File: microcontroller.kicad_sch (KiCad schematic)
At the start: 22 parts, among them J1 TC2030-IDC, U1 ESP32-WROVER

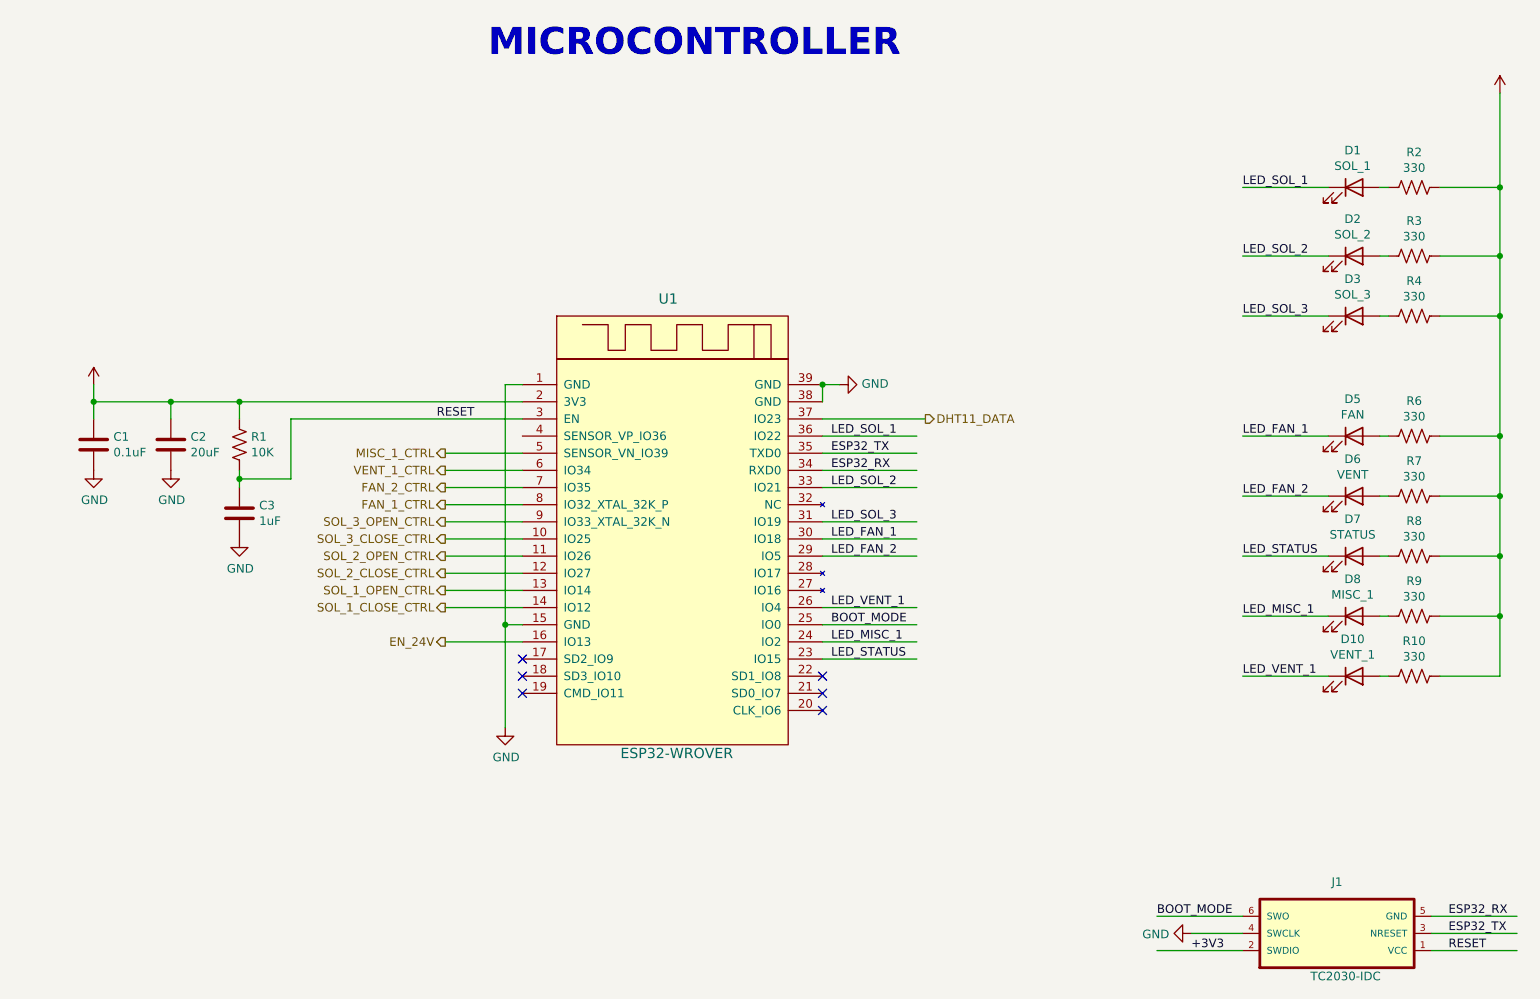
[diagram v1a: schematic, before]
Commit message: Added clamping diode for 24V net.
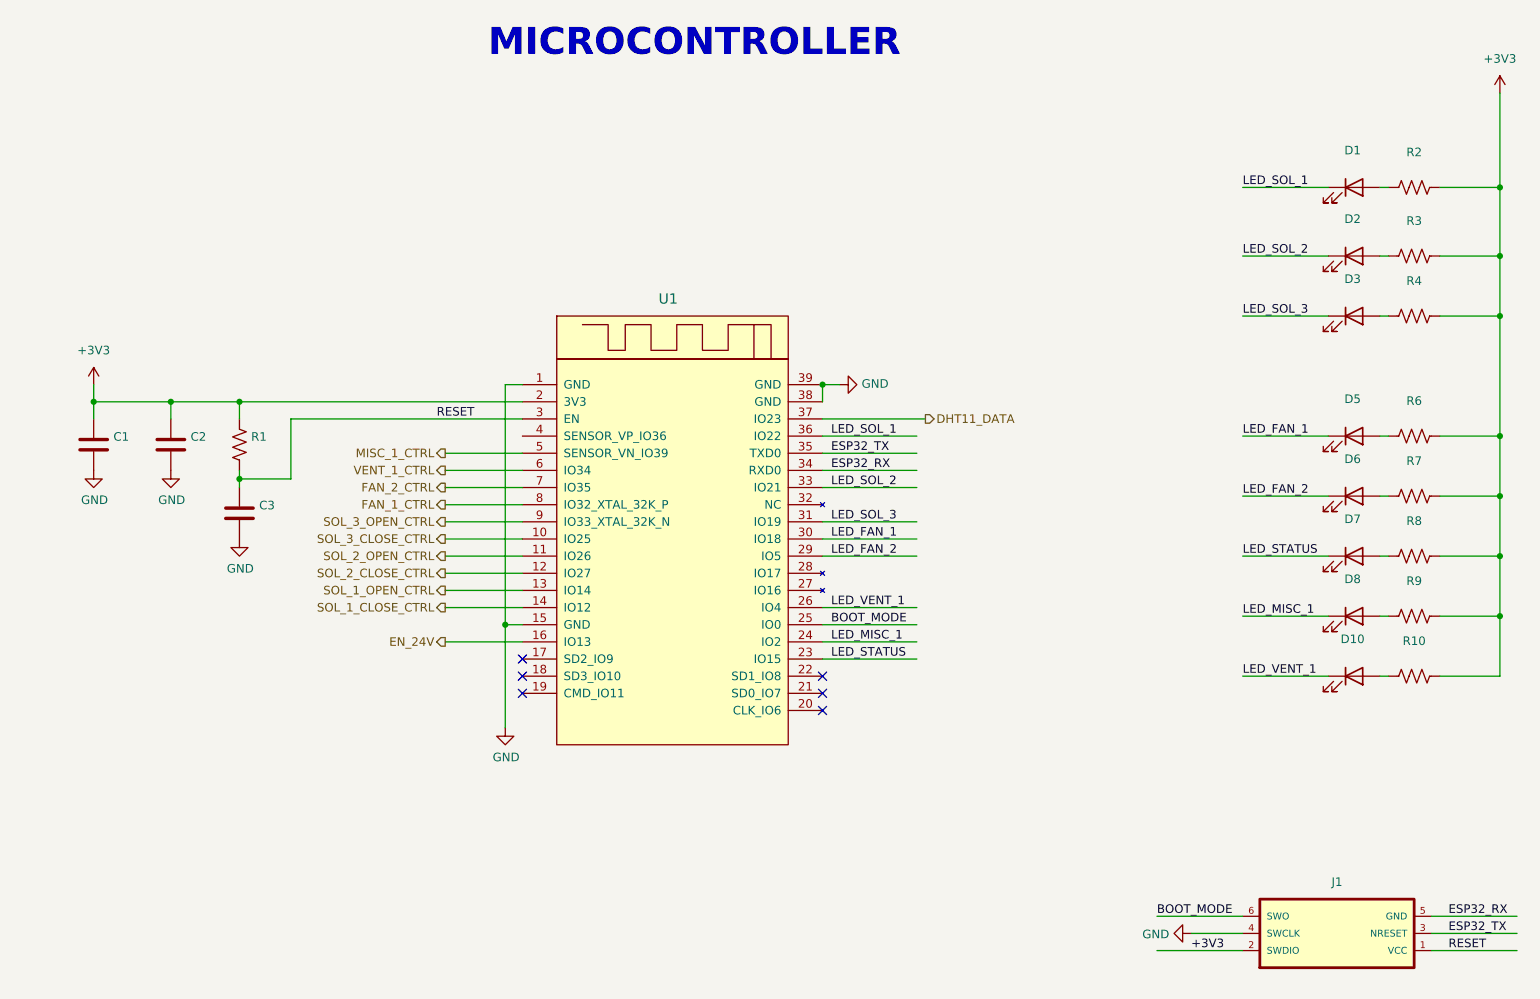
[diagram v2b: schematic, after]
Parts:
- C1: value 0.1uF -> (none); footprint Capacitor_SMD:C_0805_2012Metric -> (none)
- C2: value 20uF -> (none); footprint Capacitor_SMD:C_0805_2012Metric -> (none)
- C3: value 1uF -> (none); footprint Capacitor_SMD:C_0805_2012Metric -> (none)
- D1: value SOL_1 -> (none); footprint LED_SMD:LED_0805_2012Metric -> (none)
- D10: value VENT_1 -> (none); footprint LED_SMD:LED_0805_2012Metric -> (none)
- D2: value SOL_2 -> (none); footprint LED_SMD:LED_0805_2012Metric -> (none)
- D3: value SOL_3 -> (none); footprint LED_SMD:LED_0805_2012Metric -> (none)
- D5: value FAN -> (none); footprint LED_SMD:LED_0805_2012Metric -> (none)
- D6: value VENT -> (none); footprint LED_SMD:LED_0805_2012Metric -> (none)
- D7: value STATUS -> (none); footprint LED_SMD:LED_0805_2012Metric -> (none)
- D8: value MISC_1 -> (none); footprint LED_SMD:LED_0805_2012Metric -> (none)
- J1: value TC2030-IDC -> (none); footprint connector:TC2030-IDC -> (none)
- R1: value 10K -> (none); footprint Resistor_SMD:R_0805_2012Metric -> (none)
- R10, R2, R3, R4, R6, R7, R8, R9: value 330 -> (none); footprint Resistor_SMD:R_0805_2012Metric -> (none)
- U1: value ESP32-WROVER -> (none); footprint esp32-wrover:ESP32-WROVER -> (none)
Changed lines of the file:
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@@
       (effects (font (size 1.524 1.524)))
     )
-    (property "Value" "ESP32-WROVER" (id 1) (at 153.67 128.27 0)
+    (property "Value" "" (id 1) (at 153.67 128.27 0)
       (effects (font (size 1.524 1.524)))
     )
-    (property "Footprint" "esp32-wrover:ESP32-WROVER" (id 2) (at 165.1 100.33 0)
+    (property "Footprint" "" (id 2) (at 165.1 100.33 0)
       (effects (font (size 1.524 1.524)) hide)
     )
@@
       (effects (font (size 1.27 1.27)) (justify left))
     )
-    (property "Value" "20uF" (id 1) (at 81.661 83.693 0)
-      (effects (font (size 1.27 1.27)) (justify left))
-    )
-    (property "Footprint" "Capacitor_SMD:C_0805_2012Metric" (id 2) (at 79.7052 86.36 0)
+    (property "Value" "" (id 1) (at 81.661 83.693 0)
+      (effects (font (size 1.27 1.27)) (justify left))
+    )
+    (property "Footprint" "" (id 2) (at 79.7052 86.36 0)
       (effects (font (size 1.27 1.27)) hide)
     )
@@
       (effects (font (size 1.27 1.27)) (justify left))
     )
-    (property "Value" "0.1uF" (id 1) (at 70.231 83.693 0)
-      (effects (font (size 1.27 1.27)) (justify left))
-    )
-    (property "Footprint" "Capacitor_SMD:C_0805_2012Metric" (id 2) (at 68.2752 86.36 0)
+    (property "Value" "" (id 1) (at 70.231 83.693 0)
+      (effects (font (size 1.27 1.27)) (justify left))
+    )
+    (property "Footprint" "" (id 2) (at 68.2752 86.36 0)
       (effects (font (size 1.27 1.27)) hide)
     )
@@
     (in_bom yes) (on_board yes)
     (property "Reference" "D1" (id 0) (at 253.7714 38.9636 0))
-    (property "Value" "SOL_1" (id 1) (at 253.7714 41.275 0))
-    (property "Footprint" "LED_SMD:LED_0805_2012Metric" (id 2) (at 254 44.45 0)
+    (property "Value" "" (id 1) (at 253.7714 41.275 0))
+    (property "Footprint" "" (id 2) (at 254 44.45 0)
       (effects (font (size 1.27 1.27)) hide)
     )
@@
     (in_bom yes) (on_board yes)
     (property "Reference" "D2" (id 0) (at 253.7714 49.1236 0))
-    (property "Value" "SOL_2" (id 1) (at 253.7714 51.435 0))
-    (property "Footprint" "LED_SMD:LED_0805_2012Metric" (id 2) (at 254 54.61 0)
+    (property "Value" "" (id 1) (at 253.7714 51.435 0))
+    (property "Footprint" "" (id 2) (at 254 54.61 0)
       (effects (font (size 1.27 1.27)) hide)
     )
@@
     (in_bom yes) (on_board yes)
     (property "Reference" "D3" (id 0) (at 253.7714 58.0136 0))
-    (property "Value" "SOL_3" (id 1) (at 253.7714 60.325 0))
-    (property "Footprint" "LED_SMD:LED_0805_2012Metric" (id 2) (at 254 63.5 0)
+    (property "Value" "" (id 1) (at 253.7714 60.325 0))
+    (property "Footprint" "" (id 2) (at 254 63.5 0)
       (effects (font (size 1.27 1.27)) hide)
     )
@@
     (in_bom yes) (on_board yes)
     (property "Reference" "D5" (id 0) (at 253.7714 75.7936 0))
-    (property "Value" "FAN" (id 1) (at 253.7714 78.105 0))
-    (property "Footprint" "LED_SMD:LED_0805_2012Metric" (id 2) (at 254 81.28 0)
+    (property "Value" "" (id 1) (at 253.7714 78.105 0))
+    (property "Footprint" "" (id 2) (at 254 81.28 0)
       (effects (font (size 1.27 1.27)) hide)
     )
@@
     (in_bom yes) (on_board yes)
     (property "Reference" "D6" (id 0) (at 253.7714 84.6836 0))
-    (property "Value" "VENT" (id 1) (at 253.7714 86.995 0))
-    (property "Footprint" "LED_SMD:LED_0805_2012Metric" (id 2) (at 254 90.17 0)
+    (property "Value" "" (id 1) (at 253.7714 86.995 0))
+    (property "Footprint" "" (id 2) (at 254 90.17 0)
       (effects (font (size 1.27 1.27)) hide)
     )
@@
     (in_bom yes) (on_board yes)
     (property "Reference" "D7" (id 0) (at 253.7714 93.5736 0))
-    (property "Value" "STATUS" (id 1) (at 253.7714 95.885 0))
-    (property "Footprint" "LED_SMD:LED_0805_2012Metric" (id 2) (at 254 99.06 0)
+    (property "Value" "" (id 1) (at 253.7714 95.885 0))
+    (property "Footprint" "" (id 2) (at 254 99.06 0)
       (effects (font (size 1.27 1.27)) hide)
     )
@@
       (effects (font (size 1.27 1.27)) (justify left))
     )
-    (property "Value" "1uF" (id 1) (at 91.821 93.853 0)
-      (effects (font (size 1.27 1.27)) (justify left))
-    )
-    (property "Footprint" "Capacitor_SMD:C_0805_2012Metric" (id 2) (at 89.8652 96.52 0)
+    (property "Value" "" (id 1) (at 91.821 93.853 0)
+      (effects (font (size 1.27 1.27)) (justify left))
+    )
+    (property "Footprint" "" (id 2) (at 89.8652 96.52 0)
       (effects (font (size 1.27 1.27)) hide)
     )
@@
       (effects (font (size 1.27 1.27)) (justify left))
     )
-    (property "Value" "10K" (id 1) (at 90.6272 83.693 0)
-      (effects (font (size 1.27 1.27)) (justify left))
-    )
-    (property "Footprint" "Resistor_SMD:R_0805_2012Metric" (id 2) (at 89.916 82.804 90)
+    (property "Value" "" (id 1) (at 90.6272 83.693 0)
+      (effects (font (size 1.27 1.27)) (justify left))
+    )
+    (property "Footprint" "" (id 2) (at 89.916 82.804 90)
       (effects (font (size 1.27 1.27)) hide)
     )
@@
     (in_bom yes) (on_board yes)
     (property "Reference" "R2" (id 0) (at 262.89 39.243 90))
-    (property "Value" "330" (id 1) (at 262.89 41.5544 90))
-    (property "Footprint" "Resistor_SMD:R_0805_2012Metric" (id 2) (at 262.636 45.466 90)
+    (property "Value" "" (id 1) (at 262.89 41.5544 90))
+    (property "Footprint" "" (id 2) (at 262.636 45.466 90)
       (effects (font (size 1.27 1.27)) hide)
     )
@@
     (in_bom yes) (on_board yes)
     (property "Reference" "R6" (id 0) (at 262.89 76.073 90))
-    (property "Value" "330" (id 1) (at 262.89 78.3844 90))
-    (property "Footprint" "Resistor_SMD:R_0805_2012Metric" (id 2) (at 262.636 82.296 90)
+    (property "Value" "" (id 1) (at 262.89 78.3844 90))
+    (property "Footprint" "" (id 2) (at 262.636 82.296 90)
       (effects (font (size 1.27 1.27)) hide)
     )
@@
     (in_bom yes) (on_board yes)
     (property "Reference" "R7" (id 0) (at 262.89 84.963 90))
-    (property "Value" "330" (id 1) (at 262.89 87.2744 90))
-    (property "Footprint" "Resistor_SMD:R_0805_2012Metric" (id 2) (at 262.636 91.186 90)
+    (property "Value" "" (id 1) (at 262.89 87.2744 90))
+    (property "Footprint" "" (id 2) (at 262.636 91.186 90)
       (effects (font (size 1.27 1.27)) hide)
     )
@@
     (in_bom yes) (on_board yes)
     (property "Reference" "R8" (id 0) (at 262.89 93.853 90))
-    (property "Value" "330" (id 1) (at 262.89 96.1644 90))
-    (property "Footprint" "Resistor_SMD:R_0805_2012Metric" (id 2) (at 262.636 100.076 90)
+    (property "Value" "" (id 1) (at 262.89 96.1644 90))
+    (property "Footprint" "" (id 2) (at 262.636 100.076 90)
       (effects (font (size 1.27 1.27)) hide)
     )
@@
     (in_bom yes) (on_board yes)
     (property "Reference" "R4" (id 0) (at 262.89 58.293 90))
-    (property "Value" "330" (id 1) (at 262.89 60.6044 90))
-    (property "Footprint" "Resistor_SMD:R_0805_2012Metric" (id 2) (at 262.636 64.516 90)
+    (property "Value" "" (id 1) (at 262.89 60.6044 90))
+    (property "Footprint" "" (id 2) (at 262.636 64.516 90)
       (effects (font (size 1.27 1.27)) hide)
     )
@@
     (in_bom yes) (on_board yes)
     (property "Reference" "R3" (id 0) (at 262.89 49.403 90))
-    (property "Value" "330" (id 1) (at 262.89 51.7144 90))
-    (property "Footprint" "Resistor_SMD:R_0805_2012Metric" (id 2) (at 262.636 55.626 90)
+    (property "Value" "" (id 1) (at 262.89 51.7144 90))
+    (property "Footprint" "" (id 2) (at 262.636 55.626 90)
       (effects (font (size 1.27 1.27)) hide)
     )
@@
     (in_bom yes) (on_board yes)
     (property "Reference" "J1" (id 0) (at 251.46 147.32 0))
-    (property "Value" "TC2030-IDC" (id 1) (at 252.73 161.29 0))
-    (property "Footprint" "connector:TC2030-IDC" (id 2) (at 250.19 154.94 0)
+    (property "Value" "" (id 1) (at 252.73 161.29 0))
+    (property "Footprint" "" (id 2) (at 250.19 154.94 0)
       (effects (font (size 1.27 1.27)) hide)
     )
@@
     (in_bom yes) (on_board yes)
     (property "Reference" "D8" (id 0) (at 253.7714 102.4636 0))
-    (property "Value" "MISC_1" (id 1) (at 253.7714 104.775 0))
-    (property "Footprint" "LED_SMD:LED_0805_2012Metric" (id 2) (at 254 107.95 0)
+    (property "Value" "" (id 1) (at 253.7714 104.775 0))
+    (property "Footprint" "" (id 2) (at 254 107.95 0)
       (effects (font (size 1.27 1.27)) hide)
     )
@@
     (in_bom yes) (on_board yes)
     (property "Reference" "R9" (id 0) (at 262.89 102.743 90))
-    (property "Value" "330" (id 1) (at 262.89 105.0544 90))
-    (property "Footprint" "Resistor_SMD:R_0805_2012Metric" (id 2) (at 262.636 108.966 90)
+    (property "Value" "" (id 1) (at 262.89 105.0544 90))
+    (property "Footprint" "" (id 2) (at 262.636 108.966 90)
       (effects (font (size 1.27 1.27)) hide)
     )
@@
     (in_bom yes) (on_board yes)
     (property "Reference" "D10" (id 0) (at 253.7714 111.3536 0))
-    (property "Value" "VENT_1" (id 1) (at 253.7714 113.665 0))
-    (property "Footprint" "LED_SMD:LED_0805_2012Metric" (id 2) (at 254 116.84 0)
+    (property "Value" "" (id 1) (at 253.7714 113.665 0))
+    (property "Footprint" "" (id 2) (at 254 116.84 0)
       (effects (font (size 1.27 1.27)) hide)
     )
@@
     (in_bom yes) (on_board yes)
     (property "Reference" "R10" (id 0) (at 262.89 111.633 90))
-    (property "Value" "330" (id 1) (at 262.89 113.9444 90))
-    (property "Footprint" "Resistor_SMD:R_0805_2012Metric" (id 2) (at 262.636 117.856 90)
+    (property "Value" "" (id 1) (at 262.89 113.9444 90))
+    (property "Footprint" "" (id 2) (at 262.636 117.856 90)
       (effects (font (size 1.27 1.27)) hide)
     )
@@
       (effects (font (size 1.27 1.27)) hide)
     )
-    (property "Value" "" (id 1) (at 67.31 68.58 0))
+    (property "Value" "+3V3" (id 1) (at 67.31 68.58 0))
     (property "Footprint" "" (id 2) (at 67.31 73.66 0)
       (effects (font (size 1.27 1.27)) hide)
@@
       (effects (font (size 1.27 1.27)) hide)
     )
-    (property "Value" "" (id 1) (at 275.59 25.4 0))
+    (property "Value" "+3V3" (id 1) (at 275.59 25.4 0))
     (property "Footprint" "" (id 2) (at 275.59 30.48 0)
       (effects (font (size 1.27 1.27)) hide)

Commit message: Continued with layout.
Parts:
- added SW1: (no value), symbol Switch:SW_Push
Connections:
- net GND: now also SW1.1
- net RESET: now also SW1.2
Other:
- moved on the sheet: C1, C2, C3, R1
